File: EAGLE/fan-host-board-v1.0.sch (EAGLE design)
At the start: 38 parts, among them J8 QWIIC_RIGHT_ANGLE, J9 QWIIC_RIGHT_ANGLE, Q1 2N3904, U1 AMC6821-Q1QSOP-16N, U3 AP2112K-3.3

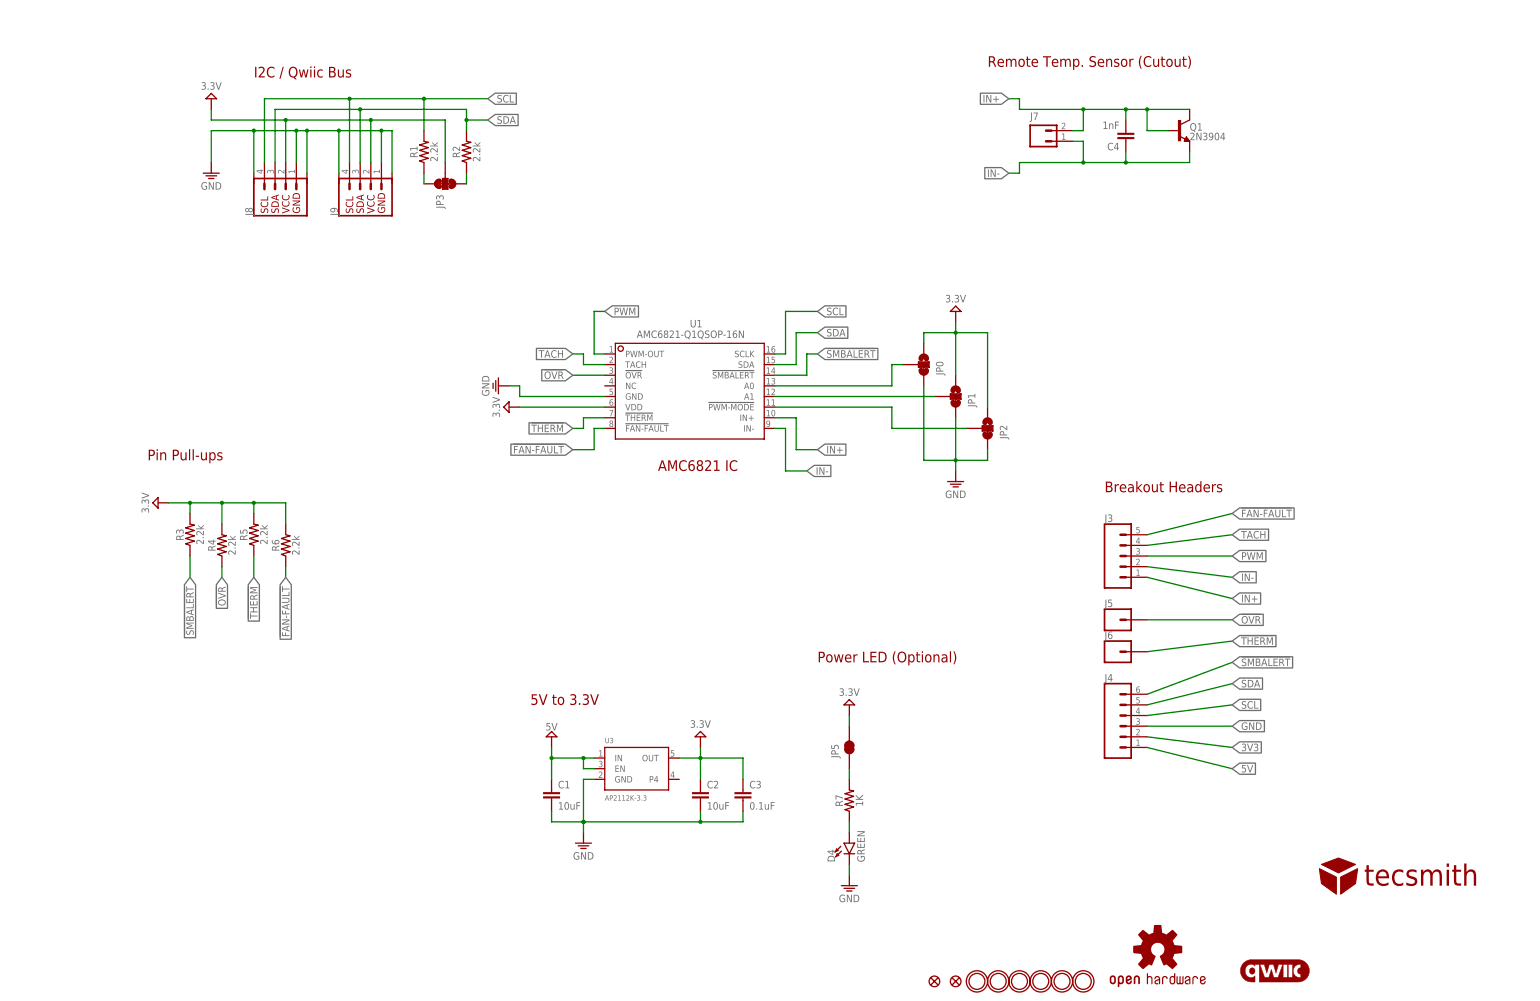
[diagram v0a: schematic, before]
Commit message: v3 upload - split into 2 boards
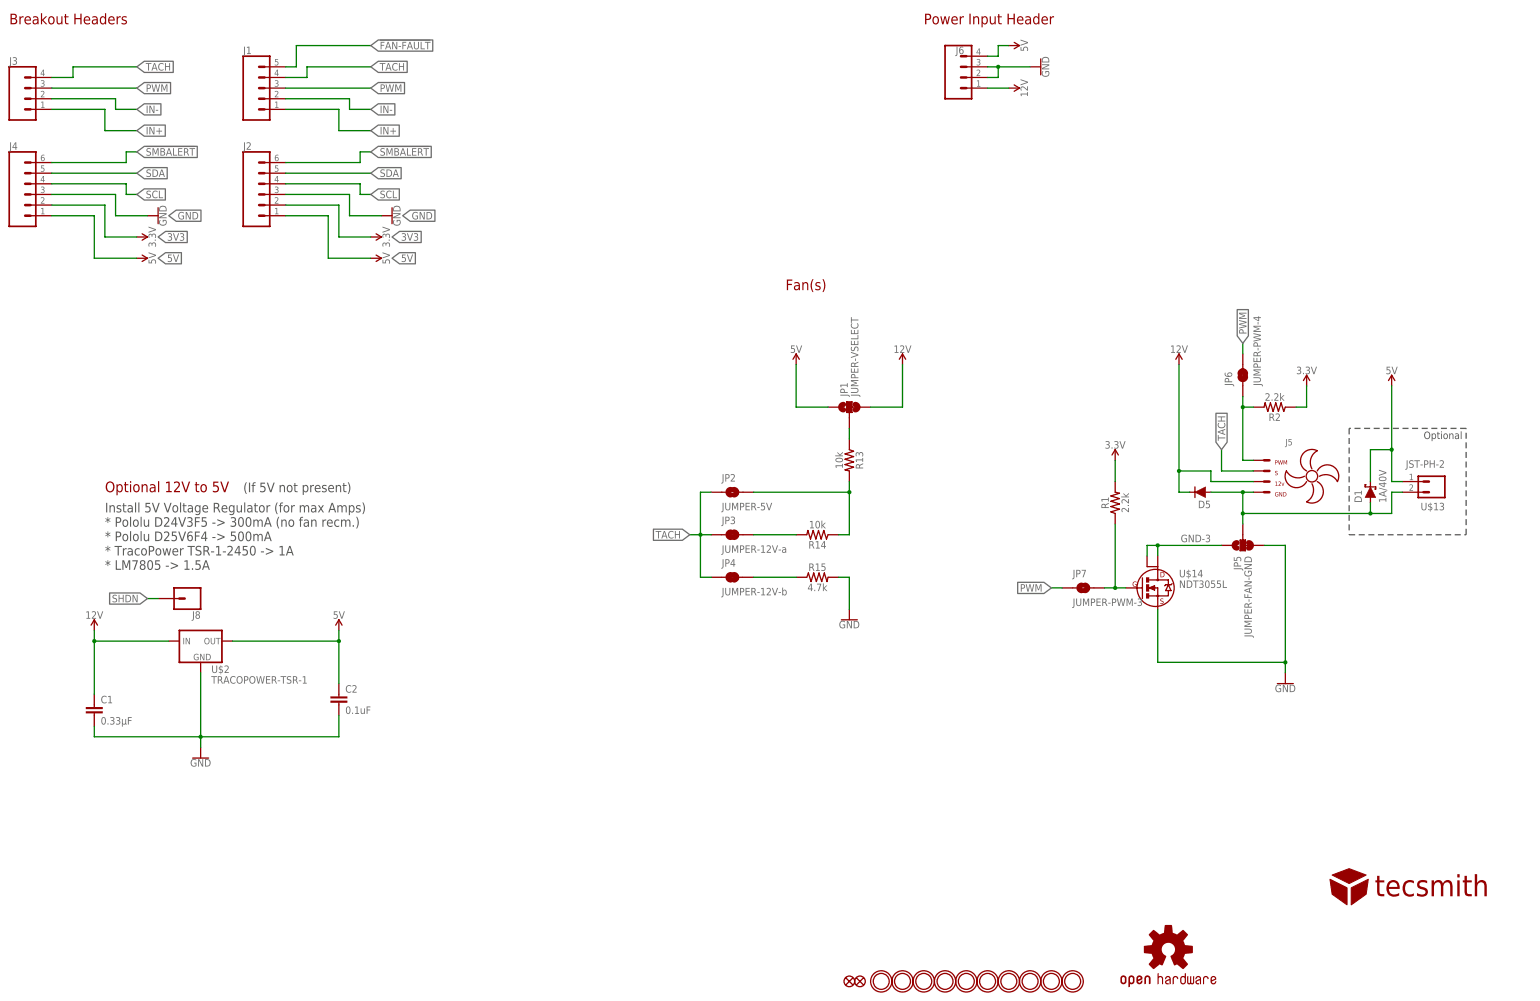
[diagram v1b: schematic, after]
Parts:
- removed C3: 0.1uF, SparkFun-Capacitors:0.1UF-0603-25V-5%
- removed C4: 1nF, SparkFun-Capacitors:1.0NF/1000PF-0603-50V-10%
- removed D4: GREEN, SparkFun-LED:LED-GREEN0603
- removed J7: (no value), VinoRodrigues_Custom_Eagle:CONN_02
- removed J9: QWIIC_RIGHT_ANGLE, VinoRodrigues_Custom_Eagle:QWIIC_CONNECTOR_GNDJS-1MM
- removed JP0: JUMPER-SMT_3_1-NC_TRACE_SILK, SparkFun-Jumpers:JUMPER-SMT_3_1-NC_TRACE_SILK
- removed LOGO2: QWIIC_LOGO_6MM, SparkFun-Aesthetics:QWIIC_LOGO_6MM
- removed Q1: 2N3904, SparkFun-DiscreteSemi:TRANS_NPN-MMBTA42
- removed R3, R4, R5, R6: 2.2k, SparkFun-Resistors:2.2KOHM-0603-1/10W-1%
- removed R7: 1K, SparkFun-Resistors:RESISTOR0805
- removed U1: AMC6821-Q1QSOP-16N, VinoRodrigues_Custom_Eagle:AMC6821-Q1QSOP-16N
- removed U3: AP2112K-3.3, microbuilder:VREG_SOT23-5
- added D1: 1A/40V, SparkFun-DiscreteSemi:DIODE-SCHOTTKY-SS14
- added D5: 200mA/100V, SparkFun-DiscreteSemi:DIODE-1N4148
- added J1: (no value), SparkFun-Connectors:CONN_05
- added J2: (no value), SparkFun-Connectors:CONN_06SILK_FEMALE_PTH
- added JP4: JUMPER-12V-b, SparkFun-Jumpers:JUMPER-SMT_2_NC_TRACE_SILK
- added JP6: JUMPER-PWM-4, SparkFun-Jumpers:JUMPER-SMT_2_NC_TRACE_SILK
- added JP7: JUMPER-PWM-3, VinoRodrigues_Custom_Eagle:JUMPER-SMT_2_NO_NO_SILK
- added R13, R14: 10k, SparkFun-Resistors:10KOHM-0603-1/10W-1%
- added R15: 4.7k, SparkFun-Resistors:4.7KOHM-0603-1/10W-1%
- added U$11, U$12, U$3, U$6: MOUNTINGHOLE2.5, microbuilder:MOUNTINGHOLE2.5
- added U$13: JST-PH-2, VinoRodrigues_Custom_Eagle:JST-PH-2
- added U$14: NDT3055L, VinoRodrigues_Custom_Eagle:NDT3055L
- added U$2: TRACOPOWER-TSR-1, VinoRodrigues_Custom_Eagle:TRACOPOWER-TSR-1
- C1: value 10uF -> 0.33µF; device SparkFun-Capacitors:10UF-0603-6.3V-20% -> SparkFun-Capacitors:0.33UF/330NF-0805-50V-10%
- C2: value 10uF -> 0.1uF; device SparkFun-Capacitors:10UF-0603-6.3V-20% -> SparkFun-Capacitors:0.1UF-0603-25V-5%
- J3: device SparkFun-Connectors:CONN_05 -> SparkFun-Connectors:CONN_04PTH
- J5: value (none) -> KK-254-4KK-254; device SparkFun-Connectors:CONN_01 -> VinoRodrigues_Custom_Eagle:KK-254-4KK-254
- J6: device SparkFun-Connectors:CONN_01 -> SparkFun-Connectors:CONN_04SCREW
- J8: value QWIIC_RIGHT_ANGLE -> (none); device VinoRodrigues_Custom_Eagle:QWIIC_CONNECTOR_GNDJS-1MM -> SparkFun-Connectors:CONN_01PTH_NO_SILK_YES_STOP
- JP1: value JUMPER-SMT_3_1-NC_TRACE_SILK -> JUMPER-VSELECT
- JP2: value JUMPER-SMT_3_1-NC_TRACE_SILK -> JUMPER-5V; device SparkFun-Jumpers:JUMPER-SMT_3_1-NC_TRACE_SILK -> VinoRodrigues_Custom_Eagle:JUMPER-SMT_2_NO_NO_SILK
- JP3: value JUMPER-SMT_3_2-NC_TRACE_SILK -> JUMPER-12V-a; device SparkFun-Jumpers:JUMPER-SMT_3_2-NC_TRACE_SILK -> SparkFun-Jumpers:JUMPER-SMT_2_NC_TRACE_SILK
- JP5: value JUMPER-SMT_2_NC_TRACE_SILK -> JUMPER-FAN-GND; device SparkFun-Jumpers:JUMPER-SMT_2_NC_TRACE_SILK -> SparkFun-Jumpers:JUMPER-SMT_3_1-NC_TRACE_SILK
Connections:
- removed net !OVR: J5.1, R4.1, U1.!OVR
- removed net !THERM: J6.1, R5.1, U1.!THERM
- removed net N$12: JP5.1, R7.2
- removed net N$3: JP3.3, R2.1
- removed net N$8: D4.A, R7.1
- new net 12V: C1.1, D5.C, J5.2:+12VDC, J6.1, JP1.3, U$2.IN
- new net GND-3: JP5.1, U$14.D, U$14.D2
- new net GND-F: D1.A, D5.A, J5.1:GND, JP5.2, U$13.2
- new net N$2: JP7.2, R1.1, U$14.G
- new net PWM-F: J5.4:PWM, JP6.1, R2.2
- new net SHDN: J8.1
- net !FAN-FAULT: now also J1.5; no longer J3.5, R6.1, U1.!FAN-FAULT
- net !SMBALERT: now also J2.6; no longer R3.1, U1.!SMBALERT
- net 3V3: now also J2.2, R1.2, R2.1; no longer C2.1, C3.1, J8.2, J9.2, JP0.1, JP1.1, JP2.1, JP3.2, JP5.2, R3.2, R4.2, R5.2, R6.2, U1.VDD, U3.OUT
- net 5V: now also C2.1, D1.C, J2.1, J6.4, JP1.1, U$13.1, U$2.OUT; no longer C1.1, U3.EN, U3.IN
- net GND: now also J2.3, J6.2, J6.3, JP5.3, R15.2, U$14.S, U$2.GND; no longer C3.2, D4.C, J8.1, J8.NC1, J8.NC2, J9.1, J9.NC1, J9.NC2, JP0.3, JP1.3, JP2.3, U1.GND, U3.GND
- net IN+: now also J1.1; no longer C4.2, J7.2, Q1.B, Q1.C, U1.IN+
- net IN-: now also J1.2; no longer C4.1, J7.1, Q1.E, U1.IN-
- net N$1: now also JP2.2, R13.2, R14.1; no longer JP0.2, U1.A0
- net N$4: now also JP1.2, R13.1; no longer JP3.1, R1.1
- net N$5: now also JP3.2, R14.2; no longer JP2.2, U1.!PWM-MODE
- net N$6: now also JP4.2, R15.1; no longer JP1.2, U1.A1
- net PWM: now also J1.3, JP6.2, JP7.1; no longer U1.PWM-OUT
- net SCL: now also J2.4; no longer J8.4, J9.4, R1.2, U1.SCLK
- net SDA: now also J2.5; no longer J8.3, J9.3, R2.2, U1.SDA
- net TACH: now also J1.4, J5.3:TACH, JP2.1, JP3.1, JP4.1; no longer U1.TACH
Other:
- note added: "(If 5V not present)"
- note added: "Fan(s)"
- note added: "Install 5V Voltage Regulator (for max Amps) * Pololu D24V3F5 -> 300mA (no fan recm.) * Pololu D25V6F4 -> 500mA * TracoPower TSR-1-2450 -> 1A * LM7805 -> 1.5A"
- note added: "Optional"
- note added: "Optional 12V to 5V"
- note added: "Power Input Header"
- note removed: "5V to 3.3V"
- note removed: "AMC6821 IC"
- note removed: "I2C / Qwiic Bus"
- note removed: "Pin Pull-ups"
- note removed: "Power LED (Optional)"
- note removed: "Remote Temp. Sensor (Cutout)"
- moved on the sheet: C1, C2, J4, JP1, R1, R2

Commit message: fixes to the TACH lines
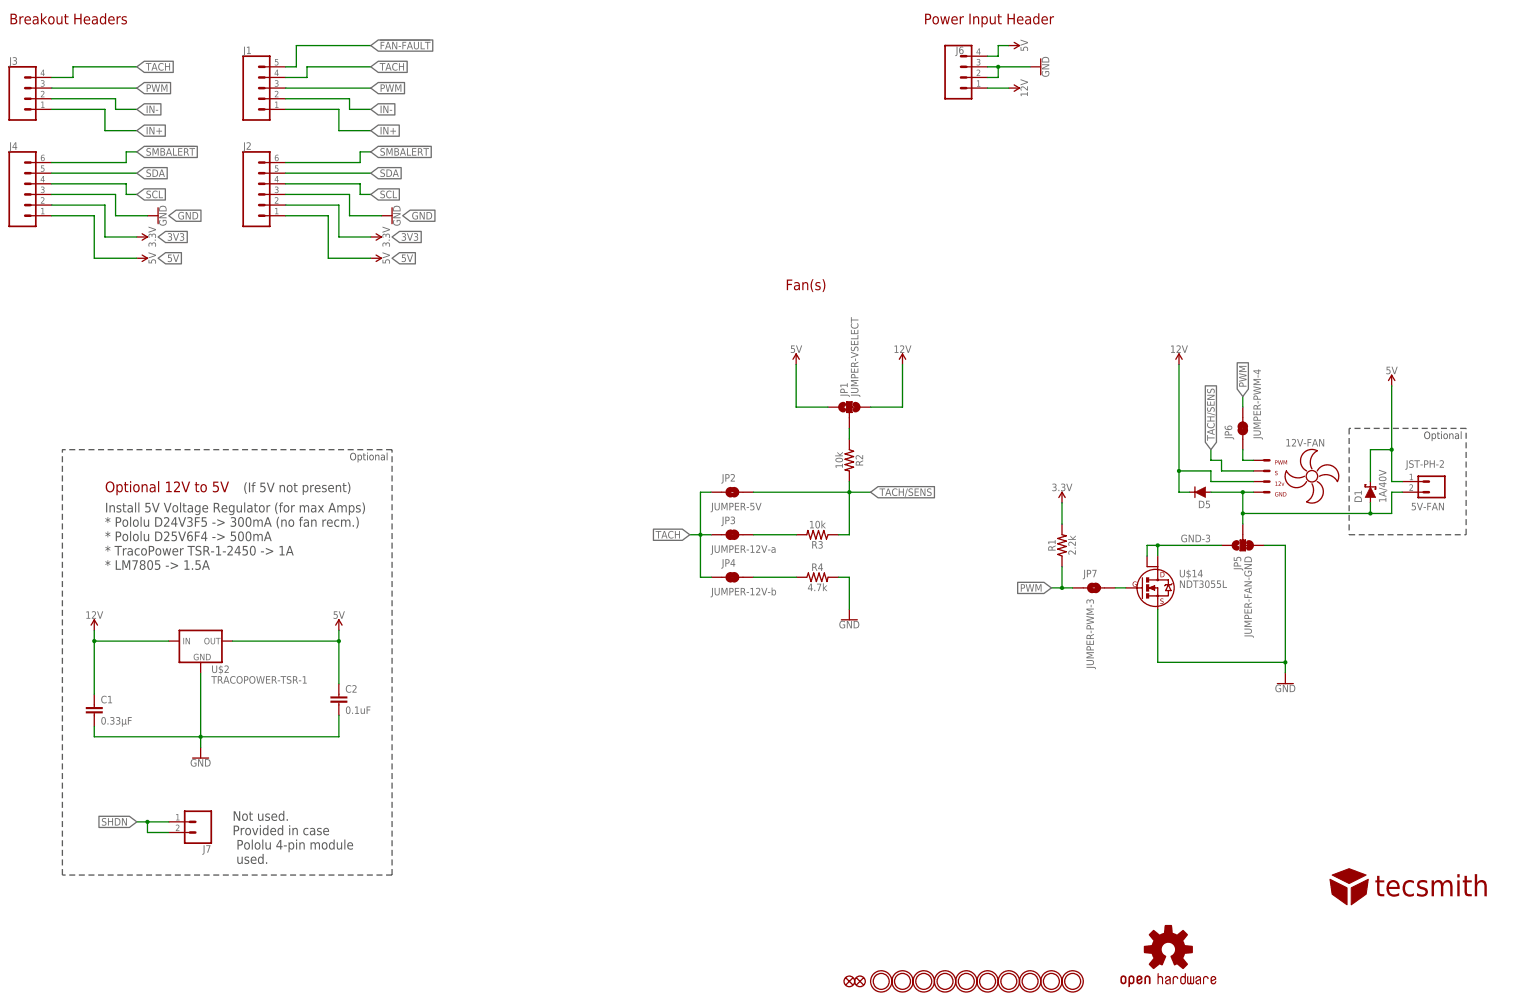
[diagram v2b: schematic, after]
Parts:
- removed J8: (no value), SparkFun-Connectors:CONN_01PTH_NO_SILK_YES_STOP
- removed R13: 10k, SparkFun-Resistors:10KOHM-0603-1/10W-1%
- added J7: (no value), SparkFun-Connectors:CONN_021X02_NO_SILK
- R2: value 2.2k -> 10k; device SparkFun-Resistors:2.2KOHM-0603-1/10W-1% -> SparkFun-Resistors:10KOHM-0603-1/10W-1%
- renumbered J5 to 12V-FAN, R14 to R3, R15 to R4, U$13 to 5V-FAN
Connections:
- removed net N$1: JP2.2, R13.2, R3.1
- new net TACH/SENS: 12V-FAN.3:TACH, JP2.2, R2.2, R3.1
- net 3V3: no longer R2.1
- net N$2: no longer R1.1
- net N$4: now also R2.1; no longer R13.1
- net PWM: now also R1.1
- net PWM-F: no longer R2.2
- net SHDN: now also J7.1, J7.2; no longer J8.1
- net TACH: no longer 12V-FAN.3:TACH
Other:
- note added: "Not used. Provided in case Pololu 4-pin module used."
- moved on the sheet: JP6, JP7, R1, R2

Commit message: minor edits
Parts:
- renumbered U$2 to VREG
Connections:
- new net ALERT: J4.6
- net !SMBALERT: no longer J4.6
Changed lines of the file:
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@@
 <part name="U$11" library="microbuilder" deviceset="MOUNTINGHOLE" device="2.5"/>
 <part name="U$12" library="microbuilder" deviceset="MOUNTINGHOLE" device="2.5"/>
-<part name="U$2" library="VinoRodrigues_Custom_Eagle" deviceset="TRACOPOWER-TSR-1" device=""/>
+<part name="VREG" library="VinoRodrigues_Custom_Eagle" deviceset="TRACOPOWER-TSR-1" device=""/>
 <part name="5V-FAN" library="VinoRodrigues_Custom_Eagle" deviceset="JST-PH-2" device=""/>
 <part name="JP3" library="SparkFun-Jumpers" deviceset="JUMPER-SMT_2_NC_TRACE" device="_SILK" package3d_urn="urn:adsk.eagle:package:39281/1" value="JUMPER-12V-a"/>
@@
 <instance part="U$11" gate="G$1" x="276.86" y="7.62" smashed="yes"/>
 <instance part="U$12" gate="G$1" x="281.94" y="7.62" smashed="yes"/>
-<instance part="U$2" gate="G$1" x="73.66" y="88.9" smashed="yes">
+<instance part="VREG" gate="G$1" x="73.66" y="88.9" smashed="yes">
 <attribute name="NAME" x="76.2" y="81.28" size="1.778" layer="95"/>
-<attribute name="VALUE" x="76.2" y="78.74" size="1.778" layer="96"/>
 </instance>
 <instance part="5V-FAN" gate="G$1" x="368.3" y="127" smashed="yes" rot="R180">
@@
 <pinref part="C1" gate="G$1" pin="1"/>
 <wire x1="48.26" y1="91.44" x2="48.26" y2="88.9" width="0.1524" layer="91"/>
-<pinref part="U$2" gate="G$1" pin="IN"/>
+<pinref part="VREG" gate="G$1" pin="IN"/>
 <wire x1="48.26" y1="88.9" x2="48.26" y2="76.2" width="0.1524" layer="91"/>
 <wire x1="66.04" y1="88.9" x2="48.26" y2="88.9" width="0.1524" layer="91"/>
@@
 <pinref part="C2" gate="G$1" pin="1"/>
 <wire x1="106.68" y1="91.44" x2="106.68" y2="88.9" width="0.1524" layer="91"/>
-<pinref part="U$2" gate="G$1" pin="OUT"/>
+<pinref part="VREG" gate="G$1" pin="OUT"/>
 <wire x1="106.68" y1="88.9" x2="106.68" y2="78.74" width="0.1524" layer="91"/>
 <wire x1="81.28" y1="88.9" x2="106.68" y2="88.9" width="0.1524" layer="91"/>
@@
 <net name="GND" class="0">
 <segment>
-<pinref part="U$2" gate="G$1" pin="GND"/>
+<pinref part="VREG" gate="G$1" pin="GND"/>
 <pinref part="GND12" gate="1" pin="GND"/>
 <wire x1="73.66" y1="81.28" x2="73.66" y2="66.04" width="0.1524" layer="91"/>
@@
 <wire x1="111.76" y1="205.74" x2="114.3" y2="205.74" width="0.1524" layer="91"/>
 <label x="114.3" y="205.74" size="1.778" layer="95" xref="yes"/>
-</segment>
-<segment>
-<pinref part="J4" gate="G$1" pin="6"/>
-<wire x1="38.1" y1="203.2" x2="55.88" y2="203.2" width="0.1524" layer="91"/>
-<wire x1="55.88" y1="203.2" x2="55.88" y2="205.74" width="0.1524" layer="91"/>
-<wire x1="55.88" y1="205.74" x2="58.42" y2="205.74" width="0.1524" layer="91"/>
-<label x="58.42" y="205.74" size="1.778" layer="95" xref="yes"/>
 </segment>
 </net>
@@
 </segment>
 </net>
+<net name="ALERT" class="0">
+<segment>
+<pinref part="J4" gate="G$1" pin="6"/>
+<wire x1="38.1" y1="203.2" x2="55.88" y2="203.2" width="0.1524" layer="91"/>
+<wire x1="55.88" y1="203.2" x2="55.88" y2="205.74" width="0.1524" layer="91"/>
+<wire x1="55.88" y1="205.74" x2="58.42" y2="205.74" width="0.1524" layer="91"/>
+<label x="58.42" y="205.74" size="1.778" layer="95" xref="yes"/>
+</segment>
+</net>

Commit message: updates
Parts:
- removed FID3, FID4: FIDUCIAL_1MM, microbuilder:FIDUCIAL_1MM
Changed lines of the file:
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@@
 <part name="U$4" library="microbuilder" deviceset="MOUNTINGHOLE" device="2.5"/>
 <part name="U$7" library="microbuilder" deviceset="MOUNTINGHOLE" device="2.5"/>
-<part name="FID3" library="microbuilder" deviceset="FIDUCIAL" device="_1MM"/>
-<part name="FID4" library="microbuilder" deviceset="FIDUCIAL" device="_1MM"/>
 <part name="U$8" library="microbuilder" deviceset="MOUNTINGHOLE" device="2.5"/>
 <part name="U$9" library="microbuilder" deviceset="MOUNTINGHOLE" device="2.5"/>
@@
 <instance part="U$4" gate="G$1" x="236.22" y="7.62" smashed="yes"/>
 <instance part="U$7" gate="G$1" x="251.46" y="7.62" smashed="yes"/>
-<instance part="FID3" gate="G$1" x="228.6" y="7.62" smashed="yes"/>
-<instance part="FID4" gate="G$1" x="231.14" y="7.62" smashed="yes"/>
 <instance part="U$8" gate="G$1" x="256.54" y="7.62" smashed="yes"/>
 <instance part="U$9" gate="G$1" x="261.62" y="7.62" smashed="yes"/>

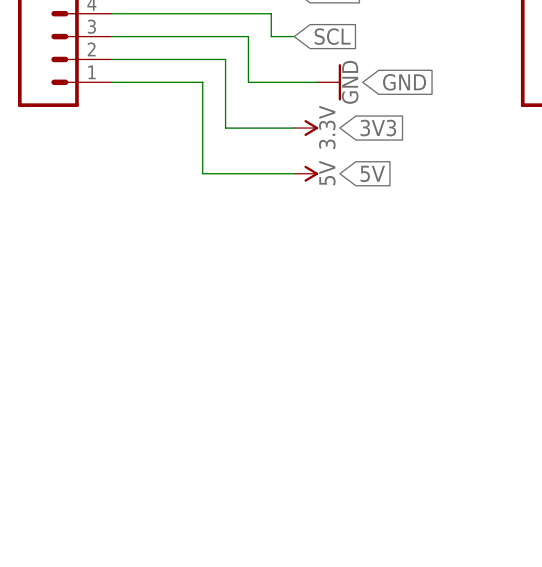
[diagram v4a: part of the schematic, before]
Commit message: added active buzzer
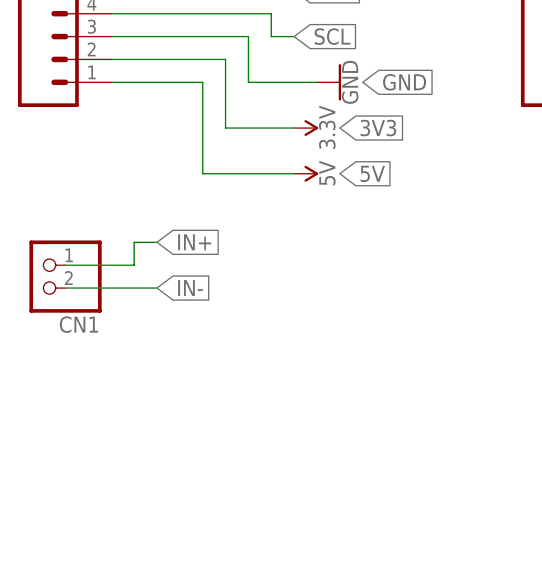
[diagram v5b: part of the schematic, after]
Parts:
- added CN1: (no value), adafruit:JST_2PIN-THM
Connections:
- net IN+: now also CN1.2
- net IN-: now also CN1.1
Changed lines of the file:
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@@
 <part name="JP6" library="SparkFun-Jumpers" deviceset="JUMPER-SMT_2_NC_TRACE" device="_SILK" package3d_urn="urn:adsk.eagle:package:39281/1" value="JUMPER-PWM-4"/>
 <part name="J7" library="SparkFun-Connectors" deviceset="CONN_02" device="1X02_NO_SILK"/>
+<part name="CN1" library="adafruit" library_urn="urn:adsk.eagle:library:420" deviceset="JST_2PIN" device="-THM" package3d_urn="urn:adsk.eagle:package:6240693/1"/>
 </parts>
 <sheets>
@@
 <attribute name="NAME" x="76.2" y="40.132" size="1.778" layer="95" font="vector" rot="R180"/>
 </instance>
+<instance part="CN1" gate="G$1" x="30.48" y="170.18" smashed="yes" rot="R180">
+<attribute name="NAME" x="36.83" y="164.465" size="1.778" layer="95" rot="R180"/>
+<attribute name="VALUE" x="36.83" y="175.26" size="1.778" layer="96" rot="R180"/>
+</instance>
 </instances>
 <busses>
@@
 <pinref part="J3" gate="J1" pin="2"/>
 </segment>
+<segment>
+<pinref part="CN1" gate="G$1" pin="1"/>
+<wire x1="33.02" y1="167.64" x2="43.18" y2="167.64" width="0.1524" layer="91"/>
+<label x="43.18" y="167.64" size="1.778" layer="95" xref="yes"/>
+</segment>
 </net>
 <net name="IN+" class="0">
@@
 <pinref part="J3" gate="J1" pin="1"/>
 </segment>
-</net>
+<segment>
+<pinref part="CN1" gate="G$1" pin="2"/>
+<wire x1="33.02" y1="170.18" x2="40.64" y2="170.18" width="0.1524" layer="91"/>
+<wire x1="40.64" y1="170.18" x2="40.64" y2="172.72" width="0.1524" layer="91"/>
+<wire x1="40.64" y1="172.72" x2="43.18" y2="172.72" width="0.1524" layer="91"/>
+<label x="43.18" y="172.72" size="1.778" layer="95" xref="yes"/>
+</segment>
+</net>
